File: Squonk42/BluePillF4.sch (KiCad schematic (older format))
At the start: 55 parts, among them J1 MH20-1, J2 MH20-1, J3 MH_RA4-1, J4 MR07C-06200, J5 U02-BFD3111B0-009, U1 AP2114HA-3.3TRG1, U2 AP2112K3.3-TRG1, U3 STM32F405RGT6, U4 SY6280, Y1 FC-12M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

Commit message: Removed R12 pull-up resistoron SDIO_D3 Added R12 resistor to connect VBUS and PA9 for VBUS_SENSE (USB Host) feature Added C18 parallel decoupling capacitor on SDCard connector Added C19 parallel decoupling capacitor on LDO U1 output
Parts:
- added C18, C19: 100n, BluePillF4 Lib:C0603, symbol CAP_0603
- R12: value 100k -> 510R
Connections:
- wire segments 261 -> 265
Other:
- moved on the sheet: C16, C6, C8, J4, U1

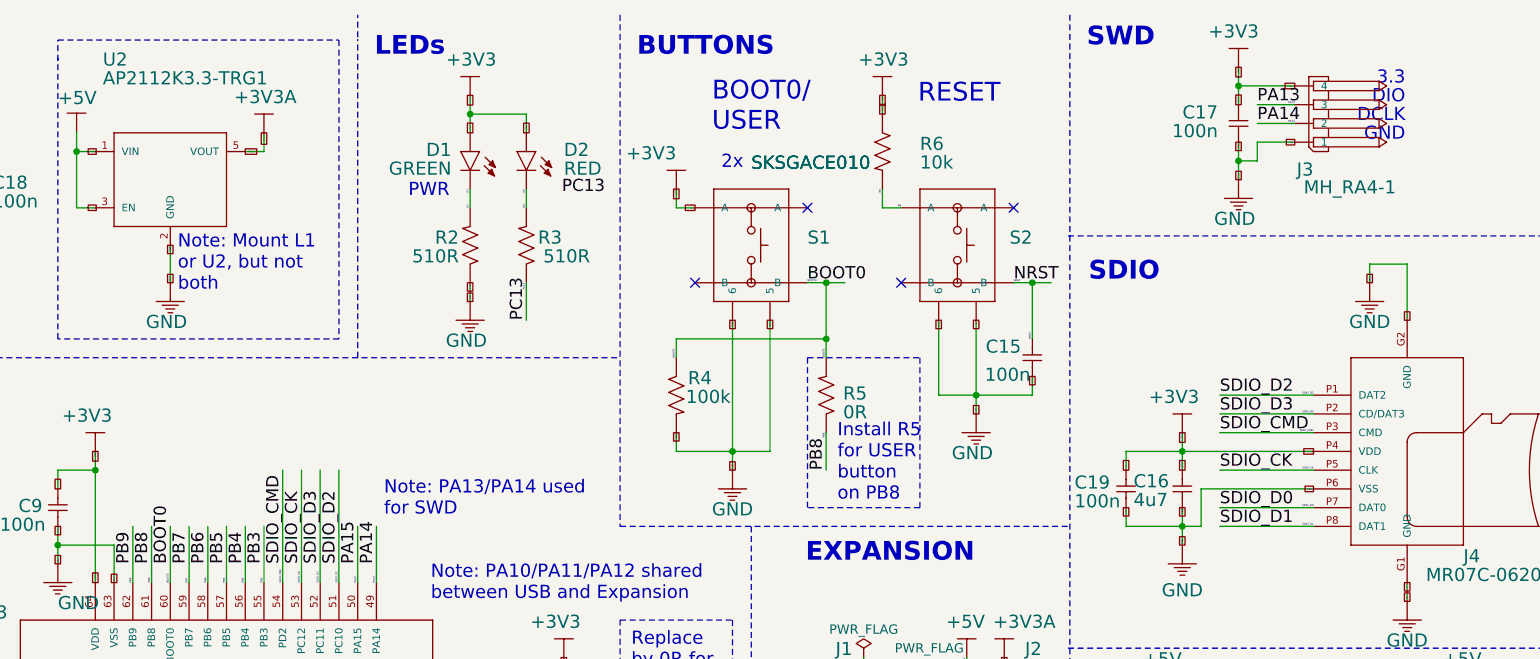
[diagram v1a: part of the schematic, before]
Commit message: Added RGB LED Added pull-down resistor on SDIO_D3 for SDCard detect feature
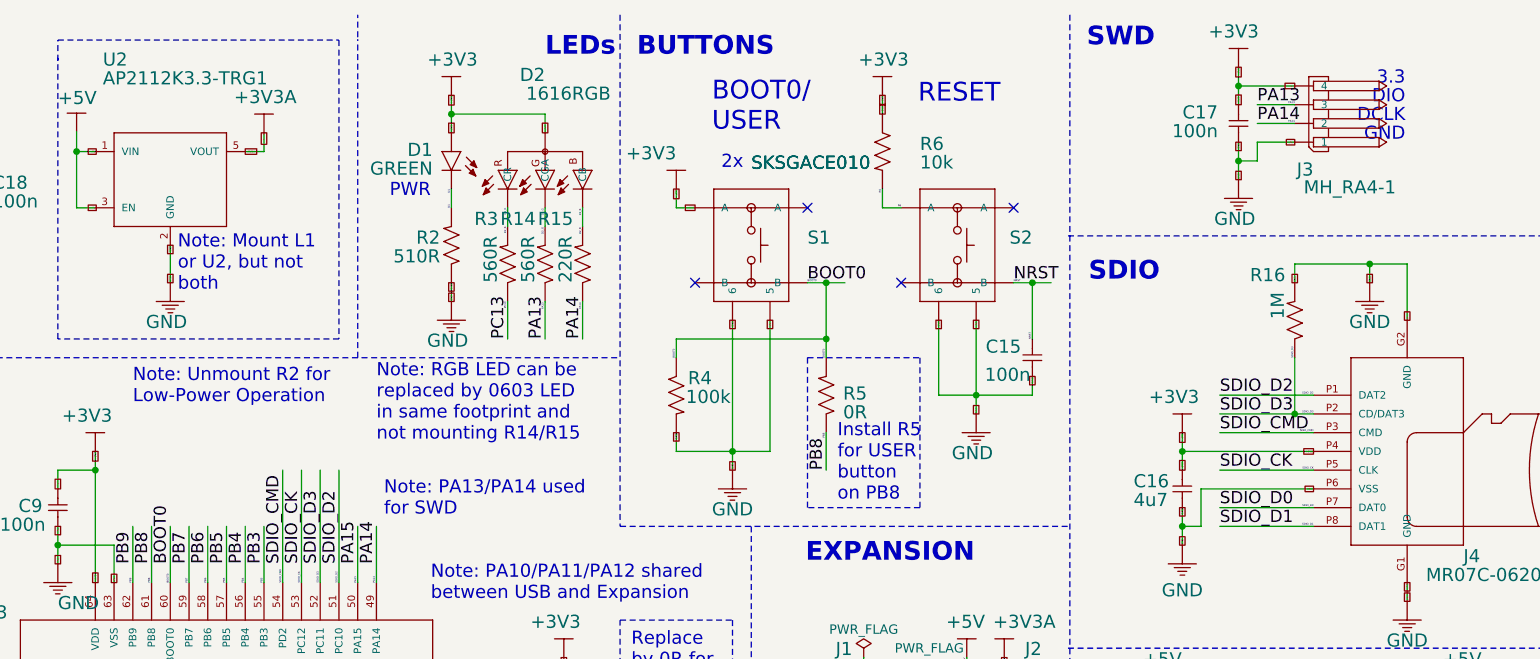
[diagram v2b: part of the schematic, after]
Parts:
- removed C19: 100n, BluePillF4 Lib:C0603, symbol CAP_0603
- removed D2: RED, BluePillF4 Lib:LED0603, symbol LED_0603
- added D2: 1616RGB, BluePillF4 Lib:1616RGB, symbol 1616RGB
- added R14: 560R, BluePillF4 Lib:R0603, symbol RES_0603
- added R15: 220R, BluePillF4 Lib:R0603, symbol RES_0603
- added R16: 1M, BluePillF4 Lib:R0603, symbol RES_0603
- R3: value 510R -> 560R
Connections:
- net labels added: D2_B, D2_G, D2_R
- net labels removed: D2
- wire segments 265 -> 269
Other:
- note added: "Note: RGB LED can be\nreplaced by 0603 LED\nin same footprint and\nnot mounting R14/R15"
- note added: "Note: Unmount R2 for\nLow-Power Operation"
- moved on the sheet: D1, R2, R3
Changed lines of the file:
@@
 LIBS:BluePillF4
 LIBS:power
-LIBS:BluePillF4-cache
 EELAYER 25 0
 EELAYER END
@@
 Sheet 1 1
 Title "BluePill F4"
-Date "2017-12-23"
+Date "2017-12-26"
 Rev "A"
 Comp "© 2017 www.stm32duino.com, All rights reserved."
@@
 Text Notes 10800 4100 0    100  ~ 20
 USB
-Text Notes 4790 700  0    100  ~ 20
+Text Notes 5700 700  0    100  ~ 20
 LEDs
 Text Notes 7260 3070 0    70   ~ 0
 Install R5\nfor USER\nbutton\non PB8
-Text Notes 5190 1450 2    70   ~ 0
+Text Notes 5090 1450 2    70   ~ 0
 PWR
 Text Notes 1090 4050 0    70   ~ 0
@@
 L LED_0603 D1
 U 1 1 5A089AB6
-P 5300 1200
-F 0 "D1" V 5350 1100 70  0000 R BNN
-F 1 "GREEN" V 5250 1100 70  0000 R BNN
-F 2 "BluePillF4 Lib:LED0603" H 5290 990 65  0001 L TNN
-F 3 "" H 5300 1200 60  0001 C CNN
-	1    5300 1200
-	0    1    -1   0
-$EndComp
-$Comp
-L LED_0603 D2
-U 1 1 5A089B7E
-P 5600 1200
-F 0 "D2" V 5650 1400 70  0000 L BNN
-F 1 "RED" V 5550 1400 70  0000 L BNN
-F 2 "BluePillF4 Lib:LED0603" H 5590 990 65  0001 L TNN
-F 3 "" H 5600 1200 60  0001 C CNN
-	1    5600 1200
+P 5200 1200
+F 0 "D1" V 5250 1100 70  0000 R BNN
+F 1 "GREEN" V 5150 1100 70  0000 R BNN
+F 2 "BluePillF4 Lib:LED0603" H 5190 990 65  0001 L TNN
+F 3 "" H 5200 1200 60  0001 C CNN
+	1    5200 1200
 	0    1    -1   0
 $EndComp
@@
 L RES_0603 R2
 U 1 1 5A08AABA
-P 5300 1700
-F 0 "R2" V 5300 1640 70  0000 R TNN
-F 1 "510R" V 5200 1640 70  0000 R TNN
-F 2 "BluePillF4 Lib:R0603" H 5290 1490 65  0001 L TNN
-F 3 "" H 5300 1700 60  0001 C CNN
-	1    5300 1700
+P 5200 1700
+F 0 "R2" V 5200 1640 70  0000 R TNN
+F 1 "510R" V 5100 1640 70  0000 R TNN
+F 2 "BluePillF4 Lib:R0603" H 5190 1490 65  0001 L TNN
+F 3 "" H 5200 1700 60  0001 C CNN
+	1    5200 1700
 	0    1    -1   0
 $EndComp
@@
 L RES_0603 R3
 U 1 1 5A08AB82
-P 5600 1700
-F 0 "R3" V 5600 1890 70  0000 R TNN
-F 1 "510R" V 5500 2040 70  0000 R TNN
-F 2 "BluePillF4 Lib:R0603" H 5590 1490 65  0001 L TNN
-F 3 "" H 5600 1700 60  0001 C CNN
-	1    5600 1700
+P 5500 1800
+F 0 "R3" V 5700 1750 70  0000 R TNN
+F 1 "560R" H 5650 1750 70  0000 R TNN
+F 2 "BluePillF4 Lib:R0603" H 5490 1590 65  0001 L TNN
+F 3 "" H 5500 1800 60  0001 C CNN
+	1    5500 1800
 	0    1    -1   0
 $EndComp
@@
 L +3V3 #SUPPLY015
 U 1 1 5A08BABE
-P 5300 900
-F 0 "#SUPPLY015" H 5300 1050 70  0001 L BNN
-F 1 "+3V3" H 5160 1050 70  0000 L BNN
-F 2 "" H 5300 900 60  0001 C CNN
-F 3 "" H 5300 900 60  0001 C CNN
-	1    5300 900
+P 5200 900
+F 0 "#SUPPLY015" H 5200 1050 70  0001 L BNN
+F 1 "+3V3" H 5060 1050 70  0000 L BNN
+F 2 "" H 5200 900 60  0001 C CNN
+F 3 "" H 5200 900 60  0001 C CNN
+	1    5200 900
 	-1   0    0    -1
 $EndComp
@@
 L GND #SUPPLY016
 U 1 1 5A08BB22
-P 5300 2000
-F 0 "#SUPPLY016" H 5300 1750 70  0001 R BNN
-F 1 "GND" H 5390 1750 70  0000 R BNN
-F 2 "" H 5300 2000 60  0001 C CNN
-F 3 "" H 5300 2000 60  0001 C CNN
-	1    5300 2000
+P 5200 2000
+F 0 "#SUPPLY016" H 5200 1750 70  0001 R BNN
+F 1 "GND" H 5290 1750 70  0000 R BNN
+F 2 "" H 5200 2000 60  0001 C CNN
+F 3 "" H 5200 2000 60  0001 C CNN
+	1    5200 2000
 	1    0    0    -1
 $EndComp
@@
 Text Label 7450 4100 0    65   ~ 0
 PC13
-Text Label 5790 1434 0    65   ~ 0
-PC13
-Text Label 5600 2100 1    65   ~ 0
+Text Label 5500 2200 1    65   ~ 0
 PC13
 Text Label 2400 4200 0    65   ~ 0
@@
 Text GLabel 7500 900  3    10   UnSpc ~ 0
 +3V3
-Text GLabel 5300 1100 1    10   UnSpc ~ 0
+Text GLabel 5200 1100 1    10   UnSpc ~ 0
 +3V3
-Text GLabel 5300 900  3    10   UnSpc ~ 0
+Text GLabel 5200 900  3    10   UnSpc ~ 0
 +3V3
-Text GLabel 5600 1100 1    10   UnSpc ~ 0
+Text GLabel 5700 1100 1    10   UnSpc ~ 0
 +3V3
 Text GLabel 9000 5500 1    10   UnSpc ~ 0
@@
 Text Label 3700 3500 1    10   ~ 0
 BOOT0
-Text Label 5300 1500 1    10   ~ 0
+Text Label 5200 1500 1    10   ~ 0
 D1
-Text Label 5300 1400 3    10   ~ 0
+Text Label 5200 1400 3    10   ~ 0
 D1
-Text Label 5600 1400 3    10   ~ 0
-D2
-Text Label 5600 1500 1    10   ~ 0
-D2
+Text Label 5500 1500 3    10   ~ 0
+D2_R
+Text Label 5500 1600 3    10   ~ 0
+D2_R
 Text Label 10400 5400 2    10   ~ 0
 DM
@@
 Text GLabel 10500 5000 1    10   UnSpc ~ 0
 GND
-Text GLabel 5300 2000 1    10   UnSpc ~ 0
+Text GLabel 5200 2000 1    10   UnSpc ~ 0
 GND
-Text GLabel 5300 1900 3    10   UnSpc ~ 0
+Text GLabel 5200 1900 3    10   UnSpc ~ 0
 GND
 Text GLabel 8300 2400 3    10   UnSpc ~ 0
@@
 Text Label 7350 4100 0    10   ~ 0
 PC13
-Text Label 5600 1900 3    10   ~ 0
+Text Label 5500 2000 3    10   ~ 0
 PC13
 Text Label 2700 4200 2    10   ~ 0
@@
 	7500 900  7500 1000
 Wire Wire Line
-	5300 900  5300 1100
+	5200 900  5200 1100
 Wire Wire Line
-	5600 1000 5600 1100
+	5700 1000 5700 1100
 Wire Wire Line
-	5600 1000 5300 1000
-Connection ~ 5300 1000
+	5700 1000 5200 1000
+Connection ~ 5200 1000
 Wire Wire Line
 	9000 5500 9000 5400
@@
 Connection ~ 2400 1200
 Wire Wire Line
-	8800 2800 9800 2800
+	9100 2800 9800 2800
 Wire Wire Line
 	9100 2700 9100 2900
@@
 	3700 3200 3700 3500
 Wire Wire Line
-	5300 1500 5300 1400
+	5200 1500 5200 1400
 Wire Wire Line
-	5600 1400 5600 1500
+	5500 1500 5500 1600
 Wire Wire Line
 	10400 5400 9900 5400
@@
 Connection ~ 10500 4800
 Wire Wire Line
-	5300 2000 5300 1900
+	5200 2000 5200 1900
 Wire Wire Line
 	7800 2500 8300 2500
@@
 	9100 3100 9100 3300
 Wire Wire Line
-	8800 3200 9200 3200
+	9100 3200 9200 3200
 Wire Wire Line
 	9200 3200 9200 3000
@@
 	10100 1900 10100 1800
 Wire Wire Line
-	10100 1800 10300 1800
+	9700 1800 10300 1800
 Wire Wire Line
 	10300 1800 10300 2100
@@
 	7650 4100 7350 4100
 Wire Wire Line
-	5600 2100 5600 1900
+	5500 2200 5500 2000
 Wire Wire Line
 	2100 3800 2100 4200
@@
 Connection ~ 2400 1800
 $Comp
-L CAP_0603 C19
-U 1 1 5A3EF348
-P 8800 3000
-F 0 "C19" V 8875 2725 70  0000 L BNN
-F 1 "100n" V 8775 2725 70  0000 L BNN
-F 2 "BluePillF4 Lib:C0603" H 8790 2790 65  0001 L TNN
-F 3 "" H 8800 3000 60  0001 C CNN
-	1    8800 3000
-	0    1    -1   0
-$EndComp
-Wire Wire Line
-	8800 2800 8800 2900
-Wire Wire Line
-	8800 3200 8800 3100
-$Comp
 L RES_0603 R12
 U 1 1 5A3F09CB
@@
 Text GLabel 2700 1500 3    10   UnSpc ~ 0
 GND
-Text GLabel 8800 2900 1    10   UnSpc ~ 0
-+3V3
-Text GLabel 8800 3100 3    10   UnSpc ~ 0
-GND
 Text GLabel 2400 6200 0    10   UnSpc ~ 0
 AGND
 Text GLabel 2900 6200 2    10   UnSpc ~ 0
 GND
+$Comp
+L 1616RGB D2
+U 1 1 5A426D49
+P 5700 1400
+F 0 "D2" V 6350 1400 70  0000 L BNN
+F 1 "1616RGB" V 6250 1050 70  0000 L BNN
+F 2 "BluePillF4 Lib:1616RGB" H 5730 1550 20  0001 C CNN
+F 3 "" H 5700 1400 60  0001 C CNN
+	1    5700 1400
+	0    -1   -1   0
+$EndComp
+$Comp
+L RES_0603 R14
+U 1 1 5A427787
+P 5700 1800
+F 0 "R14" V 5900 1750 70  0000 R TNN
+F 1 "560R" H 5850 1750 70  0000 R TNN
+F 2 "BluePillF4 Lib:R0603" H 5690 1590 65  0001 L TNN
+F 3 "" H 5700 1800 60  0001 C CNN
+	1    5700 1800
+	0    1    -1   0
+$EndComp
+$Comp
+L RES_0603 R15
+U 1 1 5A427885
+P 5900 1800
+F 0 "R15" V 6100 1750 70  0000 R TNN
+F 1 "220R" H 6050 1750 70  0000 R TNN
+F 2 "BluePillF4 Lib:R0603" H 5890 1590 65  0001 L TNN
+F 3 "" H 5900 1800 60  0001 C CNN
+	1    5900 1800
+	0    1    -1   0
+$EndComp
+Wire Wire Line
+	5700 1600 5700 1500
+Wire Wire Line
+	5900 1600 5900 1500
+Wire Wire Line
+	5700 2000 5700 2200
+Wire Wire Line
+	5900 2000 5900 2200
+Text Label 5700 1540 1    10   ~ 0
+D2_G
+Text Label 5700 1640 1    10   ~ 0
+D2_G
+Text Label 5900 1540 1    10   ~ 0
+D2_B
+Text Label 5900 1640 1    10   ~ 0
+D2_B
+Text Label 5700 2040 1    10   ~ 0
+PA13
+Text Label 5900 2040 1    10   ~ 0
+PA14
+Text Label 5700 2200 1    65   ~ 0
+PA13
+Text Label 5900 2200 1    65   ~ 0
+PA14
+Text Notes 4800 2750 0    70   ~ 0
+Note: RGB LED can be\nreplaced by 0603 LED\nin same footprint and\nnot mounting R14/R15
+Text Notes 3500 2550 0    70   ~ 0
+Note: Unmount R2 for\nLow-Power Operation
+$Comp
+L RES_0603 R16
+U 1 1 5A42D7B9
+P 9700 2100
+F 0 "R16" V 9900 2050 70  0000 R TNN
+F 1 "1M" H 9850 2050 70  0000 R TNN
+F 2 "BluePillF4 Lib:R0603" H 9690 1890 65  0001 L TNN
+F 3 "" H 9700 2100 60  0001 C CNN
+	1    9700 2100
+	0    1    -1   0
+$EndComp
+Wire Wire Line
+	9700 1900 9700 1800
+Connection ~ 10100 1800
+Wire Wire Line
+	9700 2300 9700 2600
+Connection ~ 9700 2600
+Text GLabel 9700 1900 1    10   UnSpc ~ 0
+GND
+Text Label 9700 2300 1    10   ~ 0
+SDIO_D3
 $EndSCHEMATC

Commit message: Updated BOM (was in .gitignore) Added PDF files for schematic and layout Added component fields
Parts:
- C1: DNP (none) -> F; PARTNO (none) -> C0603_10u_X7R_10%_CER_50V; SIZE (none) -> 0603; TC (none) -> X7R; TOL (none) -> ±10%; TYPE (none) -> CER; VOLT (none) -> 6.3V
- C10, C12, C13, C15, C17, C18, C7, C9: DNP (none) -> F; PARTNO (none) -> C0603_100n_X7R_10%_CER_50V; SIZE (none) -> 0603; TC (none) -> X7R; TOL (none) -> ±10%; TYPE (none) -> CER; VOLT (none) -> 50V
- C11, C14: DNP (none) -> F; PARTNO (none) -> C0603_2u2_X7R_10%_CER_50V; SIZE (none) -> 0603; TC (none) -> X7R; TOL (none) -> ±10%; TYPE (none) -> CER; VOLT (none) -> 6.3V
- C16: PARTNO (none) -> C0603_4u7_X7R_10%_CER_50V; SIZE (none) -> 0603; TC (none) -> X7R; TOL (none) -> ±10%; TYPE (none) -> CER; VOLT (none) -> 6.3V
- C2, C3: DNP (none) -> F; PARTNO (none) -> C0603_6p8_NP0_5%_CER_50V; SIZE (none) -> 0603; TC (none) -> NP0; TOL (none) -> ±5%; TYPE (none) -> CER; VOLT (none) -> 50V
- C4, C5: DNP (none) -> F; PARTNO (none) -> C0603_20p_NP0_5%_CER_50V; SIZE (none) -> 0603; TC (none) -> NP0; TOL (none) -> ±5%; TYPE (none) -> CER; VOLT (none) -> 50V
- C6, C8: DNP (none) -> F; PARTNO (none) -> C0603_4u7_X7R_10%_CER_50V; SIZE (none) -> 0603; TC (none) -> X7R; TOL (none) -> ±10%; TYPE (none) -> CER; VOLT (none) -> 6.3V
- D1: DNP (none) -> F; PARTNO (none) -> LED0603-GREEN
- D2: DNP (none) -> F; PARTNO (none) -> LED1616-RGB
- D3: DNP (none) -> F; PARTNO (none) -> 1N5819HW; RATE (none) -> 1A; VOLT (none) -> 40V
- J1, J2: DNP (none) -> F; PARTNO (none) -> MH20-1-0.1
- J3: DNP (none) -> F; PARTNO (none) -> MH_RA4-1-0.1
- J4: DNP (none) -> F; HEIGHT (none) -> 1.9mm; PARTNO (none) -> MR07C-06200
- J5: DNP (none) -> F; PARTNO (none) -> U02-BFD3111B0-009
- L1: DNP (none) -> DNP; PARTNO (none) -> FBMH1608HM471-T; RATE (none) -> 1A; SIZE (none) -> 0603
- L2: DNP (none) -> F; PARTNO (none) -> BLM18BA470SN1D; RATE (none) -> 300mA; SIZE (none) -> 0603
- PC0, PC1, PC2, PC3, PC5, PC6, PC7: BOM (none) -> EXCLUDE; DNP (none) -> F
- R1, R4, R7: DNP (none) -> F; PARTNO (none) -> R0603_100k_5%_125mW; RATE (none) -> 125mW; SIZE (none) -> 0603; TOL (none) -> 5%
- R10, R9: DNP (none) -> F; PARTNO (none) -> R0603_22R_5%_125mW; RATE (none) -> 125mW; SIZE (none) -> 0603; TOL (none) -> 5%
- R11, R5: DNP (none) -> F; RATE (none) -> 125mW; SIZE (none) -> 0603; TOL (none) -> 5%
- R12, R14, R15, R2, R3: DNP (none) -> F; PARTNO (none) -> R0603_510R_5%_125mW; RATE (none) -> 125mW; SIZE (none) -> 0603; TOL (none) -> 5%
- R13, R6: DNP (none) -> F; PARTNO (none) -> R0603_10k_5%_125mW; RATE (none) -> 125mW; SIZE (none) -> 0603; TOL (none) -> 5%
- R16: DNP (none) -> F; PARTNO (none) -> R0603_1M_5%_125mW; RATE (none) -> 125mW; SIZE (none) -> 0603; TOL (none) -> 5%
- R8: DNP (none) -> DNP; PARTNO (none) -> R0603_1k5_5%_125mW; RATE (none) -> 125mW; SIZE (none) -> 0603; TOL (none) -> 5%
- S1, S2: DNP (none) -> F; HEIGHT (none) -> 1.4mm; PARTNO (none) -> SKSGACE010
- U1: DNP (none) -> F; HEIGHT (none) -> 1.7mm; PARTNO (none) -> AP2114HA3.3-TRG1; RATE (none) -> 1A; VOLT (none) -> 3.3V
- U2: DNP (none) -> F; HEIGHT (none) -> 1.3mm; PARTNO (none) -> AP2112K3.3-TRG1; RATE (none) -> 1A; VOLT (none) -> 3.3V
- U3: DNP (none) -> F; HEIGHT (none) -> 1.6mm; PARTNO (none) -> STM32F405RGT6
- U4: DNP (none) -> F; HEIGHT (none) -> 1.3mm; PARTNO (none) -> SY6280AAC
- Y1: CAP (none) -> 12.5pF; DNP (none) -> F; FREQ (none) -> 32.768KhZ; PARTNO (none) -> FC-12M 32.7680KA-A3; TOL (none) -> ±20ppm
- Y2: CAP (none) -> 8pF; DNP (none) -> F; FREQ (none) -> 8MHz; PARTNO (none) -> NX3225GD-8MHZ-STD-CRA-3; TOL (none) -> ±50ppm

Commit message: Corrected some BOM PARTNO for capacitors, added PARTNO for some resistors
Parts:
- C1: PARTNO C0603_10u_X7R_10%_CER_50V -> C0603_10u_X7R_10%_CER_6V3
- C11, C14: PARTNO C0603_2u2_X7R_10%_CER_50V -> C0603_2u2_X7R_10%_CER_6V3
- C16: DNP (none) -> F; PARTNO C0603_4u7_X7R_10%_CER_50V -> C0603_4u7_X7R_10%_CER_6V3
- C6, C8: PARTNO C0603_4u7_X7R_10%_CER_50V -> C0603_4u7_X7R_10%_CER_6V3
- D1: SIZE (none) -> 0603
- D2: SIZE (none) -> 1616
- R11: PARTNO (none) -> R0603_1k_5%_125mW
- R5: PARTNO (none) -> R0603_510R_5%_125mW
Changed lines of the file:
@@
 F 4 "±10%" V 1200 5900 60  0001 C CNN "TOL"
 F 5 "6.3V" V 1400 6050 60  0000 C CNN "VOLT"
-F 6 "C0603_10u_X7R_10%_CER_50V" V 1200 5900 60  0001 C CNN "PARTNO"
+F 6 "C0603_10u_X7R_10%_CER_6V3" V 1200 5900 60  0001 C CNN "PARTNO"
 F 7 "CER" V 1200 5900 60  0001 C CNN "TYPE"
 F 8 "X7R" V 1200 5900 60  0001 C CNN "TC"
@@
 F 4 "±10%" H 1400 1400 60  0001 C CNN "TOL"
 F 5 "6.3V" V 1550 1250 60  0000 C CNN "VOLT"
-F 6 "C0603_4u7_X7R_10%_CER_50V" H 1400 1400 60  0001 C CNN "PARTNO"
+F 6 "C0603_4u7_X7R_10%_CER_6V3" H 1400 1400 60  0001 C CNN "PARTNO"
 F 7 "CER" H 1400 1400 60  0001 C CNN "TYPE"
 F 8 "X7R" H 1400 1400 60  0001 C CNN "TC"
@@
 F 4 "±10%" H 2400 1400 60  0001 C CNN "TOL"
 F 5 "6.3V" V 2550 1250 60  0000 C CNN "VOLT"
-F 6 "C0603_4u7_X7R_10%_CER_50V" H 2400 1400 60  0001 C CNN "PARTNO"
+F 6 "C0603_4u7_X7R_10%_CER_6V3" H 2400 1400 60  0001 C CNN "PARTNO"
 F 7 "CER" H 2400 1400 60  0001 C CNN "TYPE"
 F 8 "X7R" H 2400 1400 60  0001 C CNN "TC"
@@
 F 4 "±10%" H 4700 6500 60  0001 C CNN "TOL"
 F 5 "6.3V" V 4550 6300 60  0000 C CNN "VOLT"
-F 6 "C0603_2u2_X7R_10%_CER_50V" H 4700 6500 60  0001 C CNN "PARTNO"
+F 6 "C0603_2u2_X7R_10%_CER_6V3" H 4700 6500 60  0001 C CNN "PARTNO"
 F 7 "CER" H 4700 6500 60  0001 C CNN "TYPE"
 F 8 "X7R" H 4700 6500 60  0001 C CNN "TC"
@@
 F 4 "±10%" H 6300 4300 60  0001 C CNN "TOL"
 F 5 "6.3V" V 6150 4150 60  0000 C CNN "VOLT"
-F 6 "C0603_2u2_X7R_10%_CER_50V" H 6300 4300 60  0001 C CNN "PARTNO"
+F 6 "C0603_2u2_X7R_10%_CER_6V3" H 6300 4300 60  0001 C CNN "PARTNO"
 F 7 "CER" H 6300 4300 60  0001 C CNN "TYPE"
 F 8 "X7R" H 6300 4300 60  0001 C CNN "TC"
@@
 F 4 "±10%" H 9100 3000 60  0001 C CNN "TOL"
 F 5 "6.3V" V 8950 3150 60  0000 C CNN "VOLT"
-F 6 "C0603_4u7_X7R_10%_CER_50V" H 9100 3000 60  0001 C CNN "PARTNO"
+F 6 "C0603_4u7_X7R_10%_CER_6V3" H 9100 3000 60  0001 C CNN "PARTNO"
 F 7 "CER" H 9100 3000 60  0001 C CNN "TYPE"
 F 8 "X7R" H 9100 3000 60  0001 C CNN "TC"
 F 9 "0603" H 9100 3000 60  0001 C CNN "SIZE"
+F 10 "F" H 9100 3000 60  0001 C CNN "DNP"
 	1    9100 3000
 	0    -1   -1   0
@@
 F 3 "" H 5200 1200 60  0001 C CNN
 F 4 "LED0603-GREEN" H 5200 1200 60  0001 C CNN "PARTNO"
-F 5 "F" H 5200 1200 60  0001 C CNN "DNP"
+F 5 "0603" H 5200 1200 60  0001 C CNN "SIZE"
+F 6 "F" H 5200 1200 60  0001 C CNN "DNP"
 	1    5200 1200
 	0    1    -1   0
@@
 F 3 "" H 7200 2500 60  0001 C CNN
 F 4 "5%" H 7200 2500 60  0001 C CNN "TOL"
-F 5 "0603" H 7200 2500 60  0001 C CNN "SIZE"
-F 6 "125mW" H 7200 2500 60  0001 C CNN "RATE"
-F 7 "F" H 7200 2500 60  0001 C CNN "DNP"
+F 5 "R0603_510R_5%_125mW" H 7200 2500 60  0001 C CNN "PARTNO"
+F 6 "0603" H 7200 2500 60  0001 C CNN "SIZE"
+F 7 "125mW" H 7200 2500 60  0001 C CNN "RATE"
+F 8 "F" H 7200 2500 60  0001 C CNN "DNP"
 	1    7200 2500
 	0    1    -1   0
@@
 F 3 "" H 9300 6300 60  0001 C CNN
 F 4 "5%" H 9300 6300 60  0001 C CNN "TOL"
-F 5 "0603" H 9300 6300 60  0001 C CNN "SIZE"
-F 6 "125mW" H 9300 6300 60  0001 C CNN "RATE"
-F 7 "F" H 9300 6300 60  0001 C CNN "DNP"
+F 5 "R0603_1k_5%_125mW" H 9300 6300 60  0001 C CNN "PARTNO"
+F 6 "0603" H 9300 6300 60  0001 C CNN "SIZE"
+F 7 "125mW" H 9300 6300 60  0001 C CNN "RATE"
+F 8 "F" H 9300 6300 60  0001 C CNN "DNP"
 	1    9300 6300
 	-1   0    0    1
@@
 F 3 "http://optoelectronics.liteon.com/upload/download/DS22-2008-0044/LTST-C19HE1WT.pdf" H 5700 1400 60  0001 C CNN
 F 4 "LED1616-RGB" H 5700 1400 60  0001 C CNN "PARTNO"
-F 5 "F" H 5700 1400 60  0001 C CNN "DNP"
+F 5 "1616" H 5700 1400 60  0001 C CNN "SIZE"
+F 6 "F" H 5700 1400 60  0001 C CNN "DNP"
 	1    5700 1400
 	0    -1   -1   0
